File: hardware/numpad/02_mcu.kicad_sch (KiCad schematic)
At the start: 0 parts

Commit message: MCU schematic sheet: RP2040 minimal system
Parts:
- added C10, C11, C15, C3, C4, C5, C6, C7, C8, C9: 100n, symbol Device:C
- added C12, C13: 1u, symbol Device:C
- added C16, C17: 27p, symbol Device:C
- added J2: Conn_01x03, symbol Connector_Generic:Conn_01x03
- added R3, R4: 27, symbol Device:R
- added R5, R6: 1k, symbol Device:R
- added R7, R8: 10k, symbol Device:R
- added SW1: BOOTSEL, symbol Switch:SW_Push
- added SW2: RESET, symbol Switch:SW_Push
- added U3: RP2040, Package_DFN_QFN:QFN-56-1EP_7x7mm_P0.4mm_EP3.2x3.2mm, symbol MCU_RaspberryPi:RP2040
- added U4: W25Q128JVS, Package_SO:SOIC-8_5.3x5.3mm_P1.27mm, symbol Memory_Flash:W25Q128JVS
- added Y1: 12MHz, symbol Device:Crystal_GND24
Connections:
- new net: C17.1, R5.1, Y1.3
- new net: R5.2, U3.21 (XOUT)
- new net: R4.2, U3.47 (USB_DP)
- new net: R6.1, SW1.2
- new net: R6.2, R7.2, U3.56 (~{QSPI_SS}), U4.1 (~{CS})
- new net: R3.2, U3.46 (USB_DM)
- new net: C16.1, U3.20 (XIN), Y1.1
- new net: R8.2, SW2.2, U3.26 (RUN)
- new net: U3.51 (QSPI_SD3), U4.7 (~{HOLD}/~{RESET}/IO_{3})
- new net: U3.52 (QSPI_SCLK), U4.6 (CLK)
- new net: U3.53 (QSPI_SD0), U4.5 (DI/IO_{0})
- new net: U3.54 (QSPI_SD2), U4.3 (~{WP}/IO_{2})
- new net: U3.55 (QSPI_SD1), U4.2 (DO/IO_{1})
- new net +3V3: C10.1, C12.1, C15.1, C3.1, C4.1, C5.1, C6.1, C7.1, C8.1, C9.1, R7.1, R8.1, U3.1 (IOVDD), U3.10 (IOVDD), U3.22 (IOVDD), U3.33 (IOVDD), U3.42 (IOVDD), U3.43 (ADC_AVDD), U3.44 (VREG_VIN), U3.48 (USB_VDD), U3.49 (IOVDD), U4.8 (VCC)
- new net COL0: U3.15 (GPIO12)
- new net COL1: U3.16 (GPIO13)
- new net COL2: U3.17 (GPIO14)
- new net COL3: U3.18 (GPIO15)
- new net DVDD_1V1: C11.1, C13.1, U3.23 (DVDD), U3.45 (VREG_VOUT), U3.50 (DVDD)
- new net ENC_A: U3.9 (GPIO7)
- new net ENC_B: U3.11 (GPIO8)
- new net GND: C10.2, C11.2, C12.2, C13.2, C15.2, C16.2, C17.2, C3.2, C4.2, C5.2, C6.2, C7.2, C8.2, C9.2, J2.2 (Pin_2), SW1.1, SW2.1, U3.19 (TESTEN), U3.57 (GND), U4.4 (GND), Y1.2 (G), Y1.4 (G)
- new net I2C_SCL: U3.3 (GPIO1)
- new net I2C_SDA: U3.2 (GPIO0)
- new net RGB_DATA: U3.14 (GPIO11)
- new net ROW0: U3.4 (GPIO2)
- new net ROW1: U3.5 (GPIO3)
- new net ROW2: U3.6 (GPIO4)
- new net ROW3: U3.7 (GPIO5)
- new net ROW4: U3.8 (GPIO6)
- new net SWCLK: J2.1 (Pin_1), U3.24 (SWCLK)
- new net SWDIO: J2.3 (Pin_3), U3.25 (SWDIO)
- new net USB_DM: R3.1
- new net USB_DP: R4.1
- no-connect marks 0 -> 16
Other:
- note added: "`"

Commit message: matrix sheet, encoder, root hierarchy wired
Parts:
- renumbered C13 to C11, C11 to C12, C9 to C13, C15 to C14, C16 to C15, C17 to C16, C12 to C3, C8 to C4, C7 to C5, C5 to C7, C4 to C8, C3 to C9, R8 to R3, R7 to R4, R6 to R5, R3 to R6, R4 to R7, R5 to R8

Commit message: Format cleanup, titles
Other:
- note removed: "`"
- title: (none) -> RP2040 Minimal System
- moved on the sheet: C10, C11, C12, C13, C14, C15, C16, C3, C4, C5, C6, C7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

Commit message: footprints set
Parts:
- C10, C11, C12, C13, C14, C15, C16, C3, C4, C5, C6, C7, C8, C9: footprint (none) -> Capacitor_SMD:C_0603_1608Metric
- J2: footprint (none) -> Connector_PinHeader_2.54mm:PinHeader_1x03_P2.54mm_Vertical
- R3, R4, R5, R6, R7, R8: footprint (none) -> Resistor_SMD:R_0603_1608Metric
- SW1, SW2: footprint (none) -> Button_Switch_SMD:SW_SPST_PTS645Sx43SMTR92
- Y1: footprint (none) -> Crystal:Crystal_SMD_3225-4Pin_3.2x2.5mm
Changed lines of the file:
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@@
 			)
 		)
-		(property "Footprint" ""
+		(property "Footprint" "Resistor_SMD:R_0603_1608Metric"
 			(at 105.41 141.478 90)
 			(hide yes)
@@
 			)
 		)
-		(property "Footprint" ""
+		(property "Footprint" "Resistor_SMD:R_0603_1608Metric"
 			(at 105.41 103.378 90)
 			(hide yes)
@@
 			)
 		)
-		(property "Footprint" ""
+		(property "Footprint" "Resistor_SMD:R_0603_1608Metric"
 			(at 65.532 96.52 90)
 			(hide yes)
@@
 			)
 		)
-		(property "Footprint" ""
+		(property "Footprint" "Resistor_SMD:R_0603_1608Metric"
 			(at 105.41 100.838 90)
 			(hide yes)
@@
 			)
 		)
-		(property "Footprint" ""
+		(property "Footprint" "Crystal:Crystal_SMD_3225-4Pin_3.2x2.5mm"
 			(at 101.6 134.62 0)
 			(hide yes)
@@
 			)
 		)
-		(property "Footprint" ""
+		(property "Footprint" "Connector_PinHeader_2.54mm:PinHeader_1x03_P2.54mm_Vertical"
 			(at 100.33 162.56 0)
 			(hide yes)
@@
 			)
 		)
-		(property "Footprint" ""
+		(property "Footprint" "Capacitor_SMD:C_0603_1608Metric"
 			(at 98.0948 39.37 0)
 			(hide yes)
@@
 			)
 		)
-		(property "Footprint" ""
+		(property "Footprint" "Button_Switch_SMD:SW_SPST_PTS645Sx43SMTR92"
 			(at 72.39 87.63 0)
 			(hide yes)
@@
 			)
 		)
-		(property "Footprint" ""
+		(property "Footprint" "Resistor_SMD:R_0603_1608Metric"
 			(at 102.87 93.218 90)
 			(hide yes)
@@
 			)
 		)
-		(property "Footprint" ""
+		(property "Footprint" "Capacitor_SMD:C_0603_1608Metric"
 			(at 89.2048 39.37 0)
 			(hide yes)
@@
 			)
 		)
-		(property "Footprint" ""
+		(property "Footprint" "Button_Switch_SMD:SW_SPST_PTS645Sx43SMTR92"
 			(at 93.98 88.9 0)
 			(hide yes)
@@
 			)
 		)
-		(property "Footprint" ""
+		(property "Footprint" "Capacitor_SMD:C_0603_1608Metric"
 			(at 106.3752 74.93 0)
 			(hide yes)
@@
 			)
 		)
-		(property "Footprint" ""
+		(property "Footprint" "Capacitor_SMD:C_0603_1608Metric"
 			(at 145.7452 62.23 0)
 			(hide yes)
@@
 			)
 		)
-		(property "Footprint" ""
+		(property "Footprint" "Resistor_SMD:R_0603_1608Metric"
 			(at 61.722 96.52 90)
 			(hide yes)
@@
 			)
 		)
-		(property "Footprint" ""
+		(property "Footprint" "Capacitor_SMD:C_0603_1608Metric"
 			(at 93.6752 137.16 0)
 			(hide yes)
@@
 			)
 		)
-		(property "Footprint" ""
+		(property "Footprint" "Capacitor_SMD:C_0603_1608Metric"
 			(at 124.7648 39.37 0)
 			(hide yes)
@@
 			)
 		)
-		(property "Footprint" ""
+		(property "Footprint" "Capacitor_SMD:C_0603_1608Metric"
 			(at 89.8652 147.32 0)
 			(hide yes)
@@
 			)
 		)
-		(property "Footprint" ""
+		(property "Footprint" "Capacitor_SMD:C_0603_1608Metric"
 			(at 80.3148 39.37 0)
 			(hide yes)
@@
 			)
 		)
-		(property "Footprint" ""
+		(property "Footprint" "Capacitor_SMD:C_0603_1608Metric"
 			(at 145.7452 44.45 0)
 			(hide yes)
@@
 			)
 		)
-		(property "Footprint" ""
+		(property "Footprint" "Capacitor_SMD:C_0603_1608Metric"
 			(at 120.3452 62.23 0)
 			(hide yes)
@@
 			)
 		)
-		(property "Footprint" ""
+		(property "Footprint" "Capacitor_SMD:C_0603_1608Metric"
 			(at 115.8748 39.37 0)
 			(hide yes)
@@
 			)
 		)
-		(property "Footprint" ""
+		(property "Footprint" "Capacitor_SMD:C_0603_1608Metric"
 			(at 158.4452 63.5 0)
 			(hide yes)
@@
 			)
 		)
-		(property "Footprint" ""
+		(property "Footprint" "Capacitor_SMD:C_0603_1608Metric"
 			(at 46.6852 97.79 0)
 			(hide yes)
@@
 			)
 		)
-		(property "Footprint" ""
+		(property "Footprint" "Capacitor_SMD:C_0603_1608Metric"
 			(at 106.9848 39.37 0)
 			(hide yes)

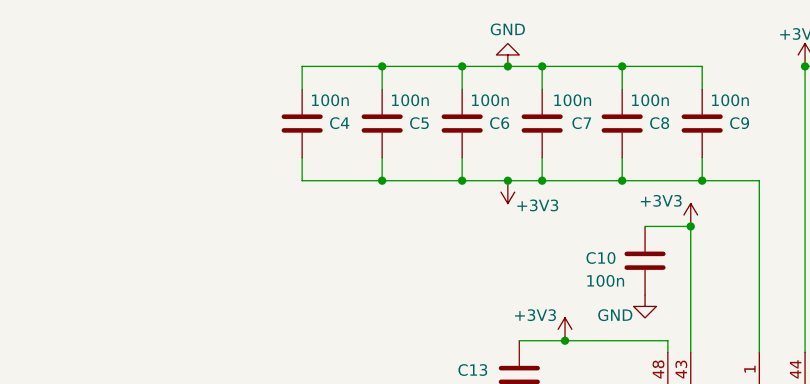
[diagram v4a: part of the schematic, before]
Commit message: throughholes added/bottom board extended, c3/c5/c11 schem value fixed
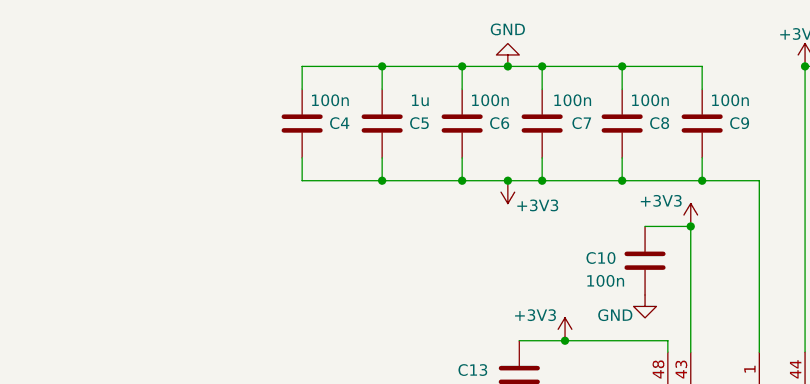
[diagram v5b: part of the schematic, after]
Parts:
- C5: value 100n -> 1u
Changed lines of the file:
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@@
 			)
 		)
-		(property "Value" "100n"
+		(property "Value" "1u"
 			(at 95.504 40.64 0)
 			(show_name no)
